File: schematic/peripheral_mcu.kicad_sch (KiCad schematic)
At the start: 46 parts, among them M1 Motor_Servo, M2 Motor_Servo, M3 Motor_DC, M4 Motor_DC, M5 Motor_DC, M6 Motor_DC, Q1 LTR-3208E, Q2 LTR-3208E, Q3 LTR-3208E, Q4 LTR-3208E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

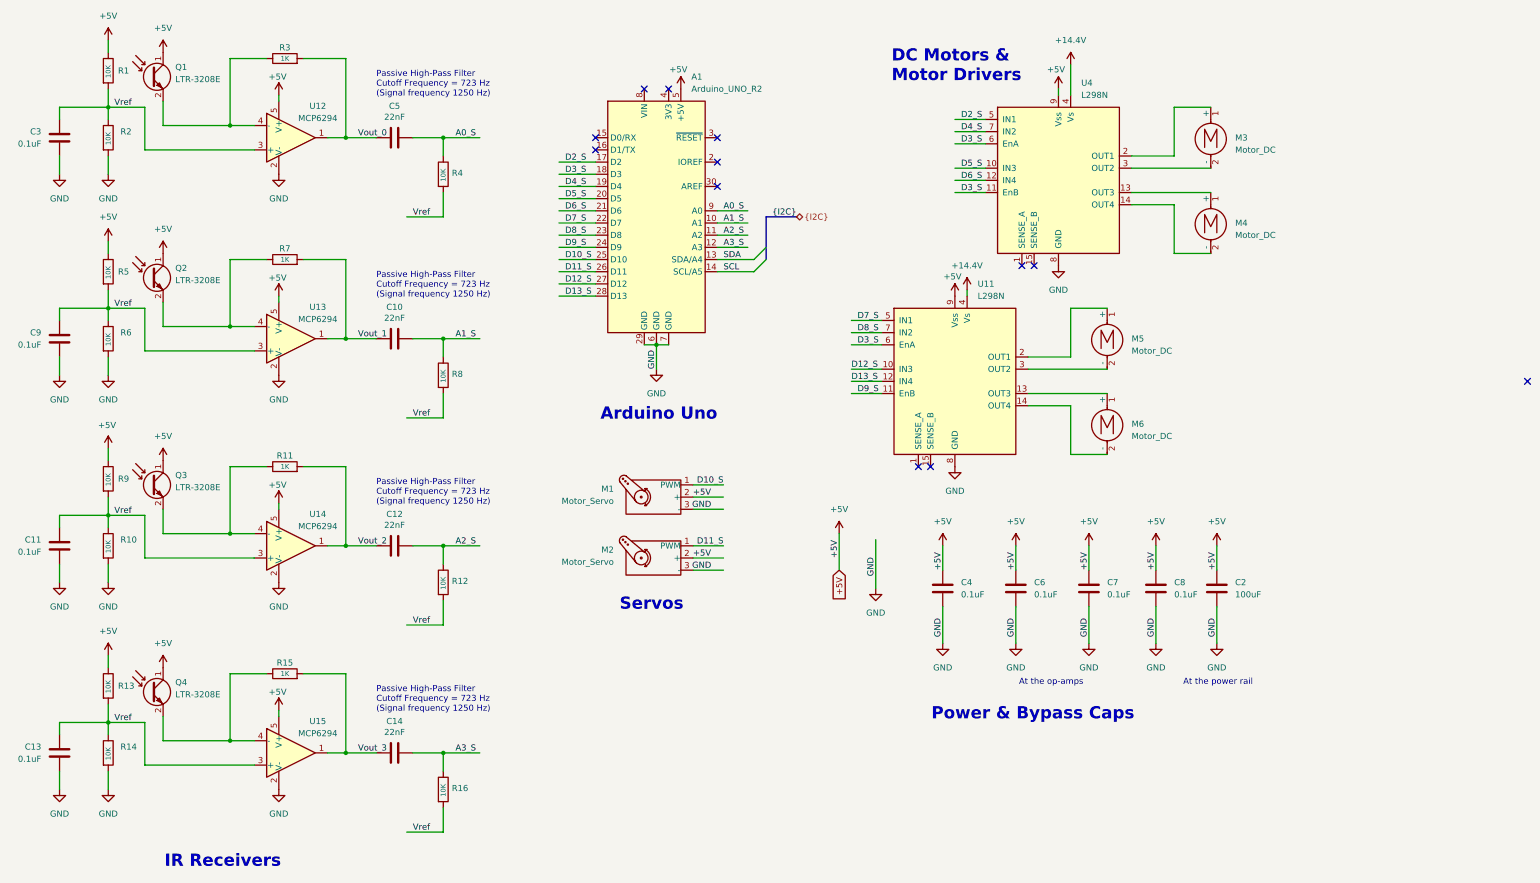
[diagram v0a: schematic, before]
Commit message: update schematic
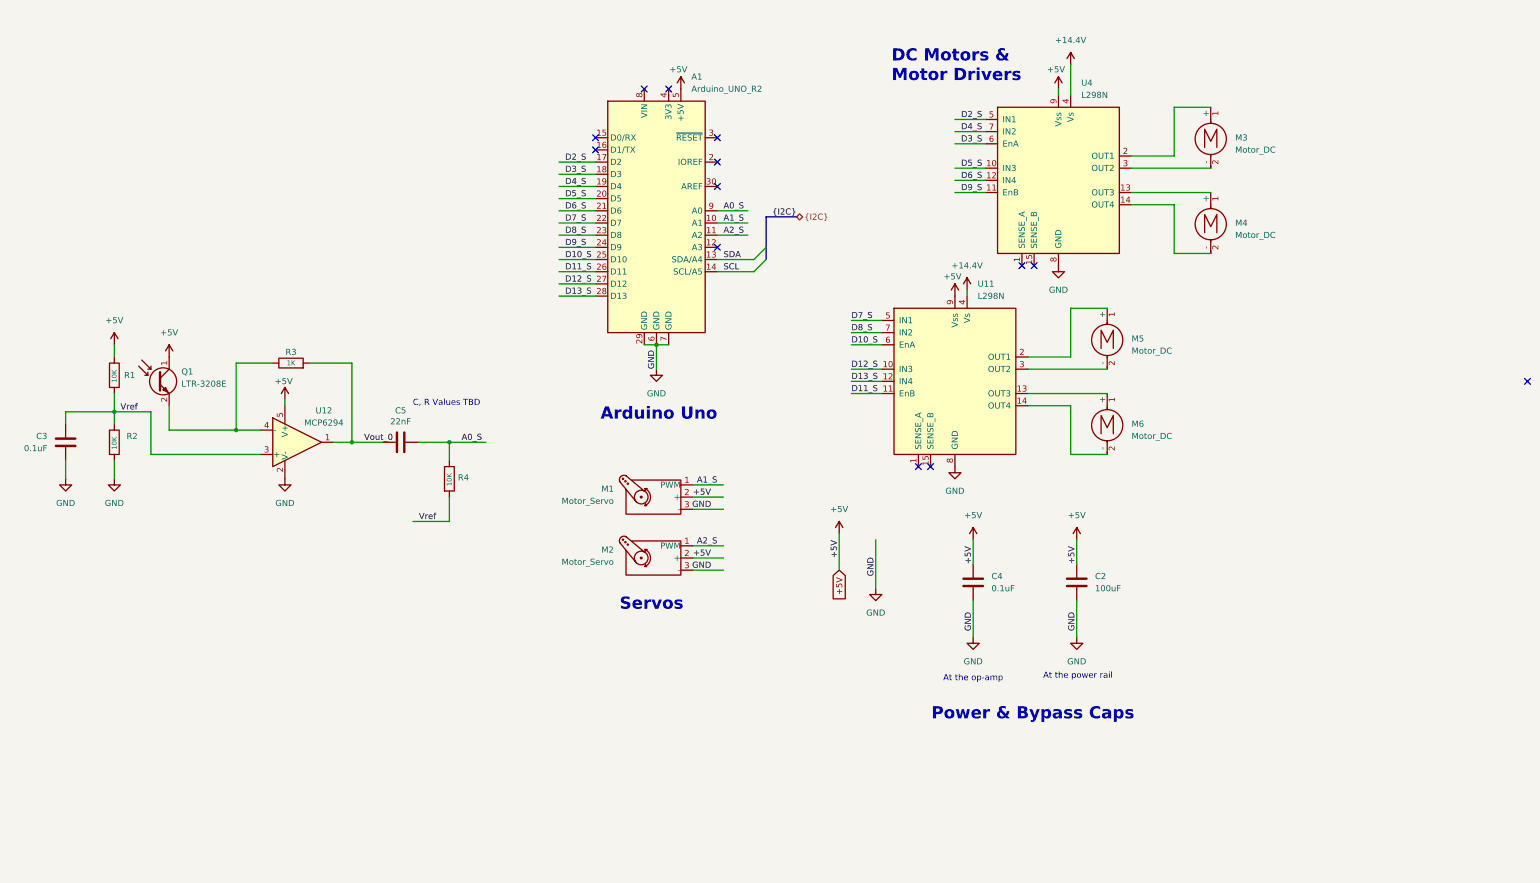
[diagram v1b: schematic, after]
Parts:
- removed C10, C12, C14: 22nF, symbol Device:C
- removed C11, C13, C6, C7, C8, C9: 0.1uF, symbol Device:C
- removed Q2, Q3, Q4: LTR-3208E, symbol Device:Q_Photo_NPN_CE
- removed R10, R12, R13, R14, R16, R5, R6, R8, R9: 10K, symbol Device:R
- removed R11, R15, R7: 1K, symbol Device:R
- removed U13, U14, U15: MCP6294, Package_TO_SOT_SMD:SOT-23-5, symbol Amplifier_Operational:MCP6001-OT
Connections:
- net A1_S: now also M1.1 (PWM)
- net A2_S: now also M2.1 (PWM)
- net D10_S: now also U11.6 (EnA); no longer M1.1 (PWM)
- net D11_S: now also U11.11 (EnB); no longer M2.1 (PWM)
- net D3_S: no longer U11.6 (EnA), U4.11 (EnB)
- net D9_S: now also U4.11 (EnB); no longer U11.11 (EnB)
- net A3_S: no longer names the net of A1.12 (A3)
- no-connect marks 12 -> 13
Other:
- note added: "At the op-amp"
- note added: "C, R Values TBD"
- note removed: "At the op-amps"
- note removed: "IR Receivers"
- note removed: "Passive High-Pass Filter Cutoff Frequency = 723 Hz (Signal frequency 1250 Hz)"
- moved on the sheet: C2, C3, C4, C5, Q1, R1, R2, R3, R4, U12

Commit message: updated schematic
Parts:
- removed C3, C4: 0.1uF, symbol Device:C
- removed C5: 22nF, symbol Device:C
- removed Q1: LTR-3208E, symbol Device:Q_Photo_NPN_CE
- removed R1, R2, R4: 10K, symbol Device:R
- removed R3: 1K, symbol Device:R
- removed U12: MCP6294, Package_TO_SOT_SMD:SOT-23-5, symbol Amplifier_Operational:MCP6001-OT
- renumbered A1 to A2, C2 to C6, U4 to U12, U11 to U13
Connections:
- net A1_S: now also U12.10 (IN3); no longer M1.1 (PWM)
- net A2_S: now also U12.12 (IN4); no longer M2.1 (PWM)
- net D5_S: now also M1.1 (PWM); no longer U12.10 (IN3)
- net D6_S: now also M2.1 (PWM); no longer U12.12 (IN4)
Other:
- note added: "TPU Arm"
- note added: "Track gate"
- note removed: "At the op-amp"
- note removed: "C, R Values TBD"
- moved on the sheet: A2, C6, M1, M2, M3, M4, M5, M6, U12, U13

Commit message: update schematics
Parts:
- M1, M2: value Motor_Servo -> Motor_Pervo
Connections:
- net A0_S renamed A0_P
- net A1_S renamed A1_P
- net A2_S renamed A2_P
- net D10_S renamed D10_P
- net D11_S renamed D11_P
- net D12_S renamed D12_P
- net D13_S renamed D13_P
- net D2_S renamed D2_P
- net D3_S renamed D3_P
- net D4_S renamed D4_P
- net D5_S renamed D5_P
- net D6_S renamed D6_P
- net D7_S renamed D7_P
- net D8_S renamed D8_P
- net D9_S renamed D9_P
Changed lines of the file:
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@@
 		)
 	)
-	(label "D2_S"
+	(label "D2_P"
 		(at 102.87 96.52 0)
 		(fields_autoplaced yes)
@@
 		)
 	)
-	(label "D11_S"
+	(label "D11_P"
 		(at 31.75 67.31 0)
 		(fields_autoplaced yes)
@@
 		)
 	)
-	(label "D5_S"
+	(label "D5_P"
 		(at 63.5 118.11 180)
 		(fields_autoplaced yes)
@@
 		)
 	)
-	(label "A2_S"
+	(label "A2_P"
 		(at 102.87 109.22 0)
 		(fields_autoplaced yes)
@@
 		)
 	)
-	(label "D9_S"
+	(label "D9_P"
 		(at 31.75 62.23 0)
 		(fields_autoplaced yes)
@@
 		)
 	)
-	(label "D6_S"
+	(label "D6_P"
 		(at 31.75 54.61 0)
 		(fields_autoplaced yes)
@@
 		)
 	)
-	(label "D3_S"
+	(label "D3_P"
 		(at 31.75 46.99 0)
 		(fields_autoplaced yes)
@@
 		)
 	)
-	(label "A1_S"
+	(label "A1_P"
 		(at 102.87 106.68 0)
 		(fields_autoplaced yes)
@@
 		)
 	)
-	(label "D8_S"
+	(label "D8_P"
 		(at 31.75 59.69 0)
 		(fields_autoplaced yes)
@@
 		)
 	)
-	(label "D8_S"
+	(label "D8_P"
 		(at 102.87 43.18 0)
 		(fields_autoplaced yes)
@@
 		)
 	)
-	(label "D2_S"
+	(label "D2_P"
 		(at 31.75 44.45 0)
 		(fields_autoplaced yes)
@@
 		)
 	)
-	(label "A0_S"
+	(label "A0_P"
 		(at 64.77 54.61 0)
 		(fields_autoplaced yes)
@@
 		)
 	)
-	(label "D4_S"
+	(label "D4_P"
 		(at 31.75 49.53 0)
 		(fields_autoplaced yes)
@@
 		)
 	)
-	(label "D13_S"
+	(label "D13_P"
 		(at 31.75 72.39 0)
 		(fields_autoplaced yes)
@@
 		)
 	)
-	(label "D4_S"
+	(label "D4_P"
 		(at 102.87 99.06 0)
 		(fields_autoplaced yes)
@@
 		)
 	)
-	(label "A1_S"
+	(label "A1_P"
 		(at 64.77 57.15 0)
 		(fields_autoplaced yes)
@@
 		)
 	)
-	(label "A2_S"
+	(label "A2_P"
 		(at 64.77 59.69 0)
 		(fields_autoplaced yes)
@@
 		)
 	)
-	(label "D12_S"
+	(label "D12_P"
 		(at 102.87 50.8 0)
 		(fields_autoplaced yes)
@@
 		)
 	)
-	(label "D5_S"
+	(label "D5_P"
 		(at 31.75 52.07 0)
 		(fields_autoplaced yes)
@@
 		)
 	)
-	(label "D7_S"
+	(label "D7_P"
 		(at 31.75 57.15 0)
 		(fields_autoplaced yes)
@@
 		)
 	)
-	(label "D10_S"
+	(label "D10_P"
 		(at 102.87 45.72 0)
 		(fields_autoplaced yes)
@@
 		)
 	)
-	(label "D7_S"
+	(label "D7_P"
 		(at 102.87 40.64 0)
 		(fields_autoplaced yes)
@@
 		)
 	)
-	(label "D12_S"
+	(label "D12_P"
 		(at 31.75 69.85 0)
 		(fields_autoplaced yes)
@@
 		)
 	)
-	(label "D9_S"
+	(label "D9_P"
 		(at 102.87 111.76 0)
 		(fields_autoplaced yes)
@@
 		)
 	)
-	(label "D11_S"
+	(label "D11_P"
 		(at 102.87 55.88 0)
 		(fields_autoplaced yes)
@@
 		)
 	)
-	(label "D3_S"
+	(label "D3_P"
 		(at 102.87 101.6 0)
 		(fields_autoplaced yes)
@@
 		)
 	)
-	(label "D10_S"
+	(label "D10_P"
 		(at 31.75 64.77 0)
 		(fields_autoplaced yes)
@@
 		)
 	)
-	(label "D13_S"
+	(label "D13_P"
 		(at 102.87 53.34 0)
 		(fields_autoplaced yes)
@@
 		)
 	)
-	(label "D6_S"
+	(label "D6_P"
 		(at 63.5 135.89 180)
 		(fields_autoplaced yes)
@@
 			)
 		)
-		(property "Value" "Motor_Servo"
+		(property "Value" "Motor_Pervo"
 			(at 41.91 139.2665 0)
 			(effects
@@
 			)
 		)
-		(property "Value" "Motor_Servo"
+		(property "Value" "Motor_Pervo"
 			(at 41.91 121.4865 0)
 			(effects

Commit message: update schematic to match most recent config
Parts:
- removed C6: 100uF, symbol Device:C
- renumbered M3 to M1, M4 to M2, M5 to M3, M6 to M4, M1 to M5, M2 to M6
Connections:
- net D10_P: now also M6.1 (PWM); no longer U13.6 (EnA)
- net D3_P: now also U13.11 (EnB)
- net D6_P: now also U12.11 (EnB), U13.6 (EnA); no longer M6.1 (PWM)
- net D9_P: now also M5.1 (PWM); no longer U12.11 (EnB)
- net +14.4V renamed +12V
- net A0_P: no longer names the net of A2.9 (A0)
- net D11_P: no longer names the net of A2.26 (D11)
- net D11_P: no longer U13.11 (EnB)
- net D5_P: no longer names the net of A2.20 (D5)
- net D5_P: no longer M5.1 (PWM)
- no-connect marks 13 -> 16
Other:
- note added: "Power"
- note removed: "At the power rail"
- note removed: "Power & Bypass Caps"
- moved on the sheet: A2, M1, M2, M3, M4, M5, M6, U12, U13
